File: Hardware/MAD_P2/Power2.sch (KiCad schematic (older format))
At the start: 39 parts, among them U13 XL1509-5.0, U14 XL1509-5.0, U15 AMS1117-3.3, U16 AMS1117-3.3, U17 AMS1117-3.3, U18 AMS1117-3.3

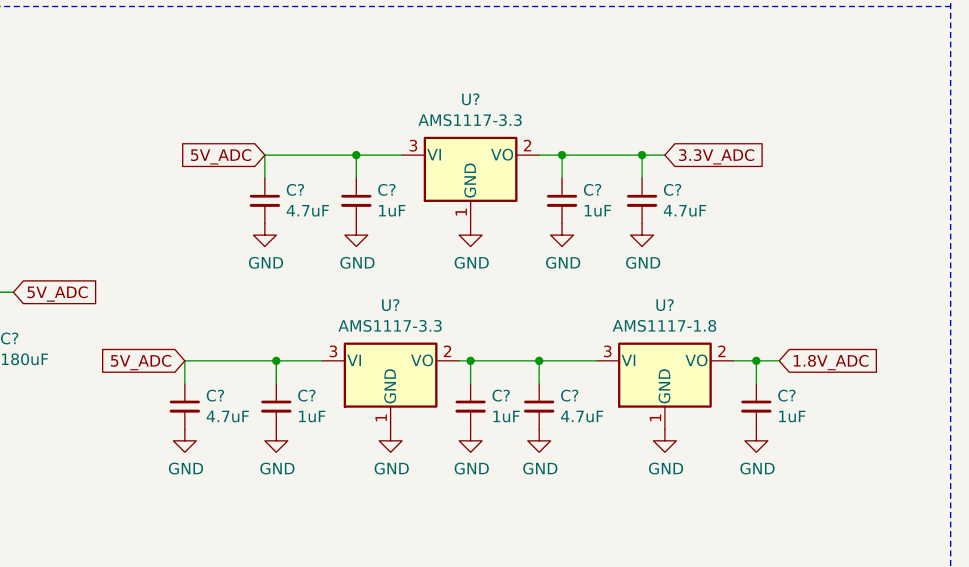
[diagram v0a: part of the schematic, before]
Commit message: changed adc to ads131
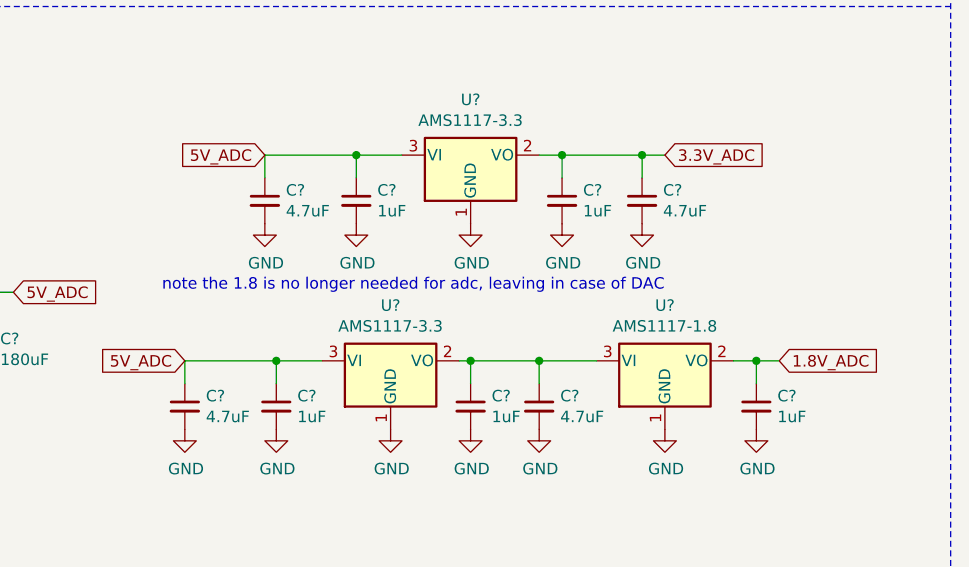
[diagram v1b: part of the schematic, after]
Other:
- note added: "note the 1.8 is no longer needed for adc, leaving in case of DAC"
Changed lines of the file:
@@
 Wire Notes Line
 	6950 500  6950 7800
+Text Notes 3500 6300 0    50   ~ 0
+note the 1.8 is no longer needed for adc, leaving in case of DAC
 $EndSCHEMATC

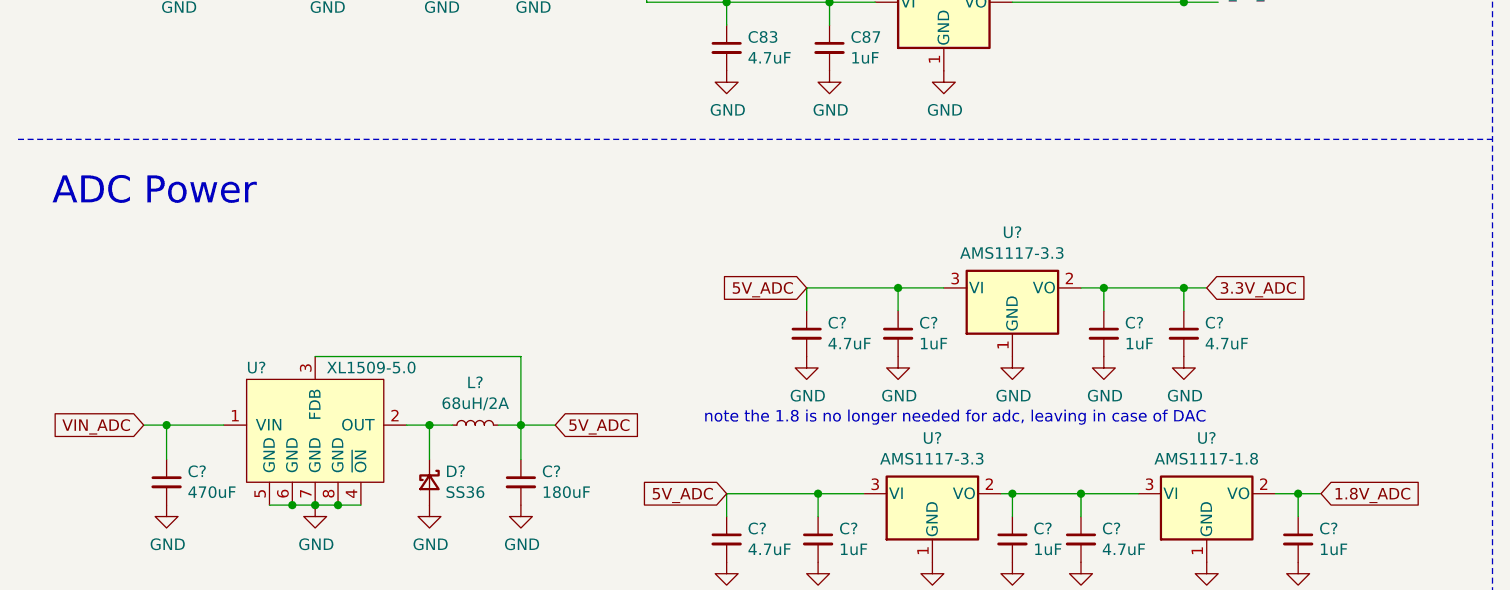
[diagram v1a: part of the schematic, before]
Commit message: finished adc, added dac
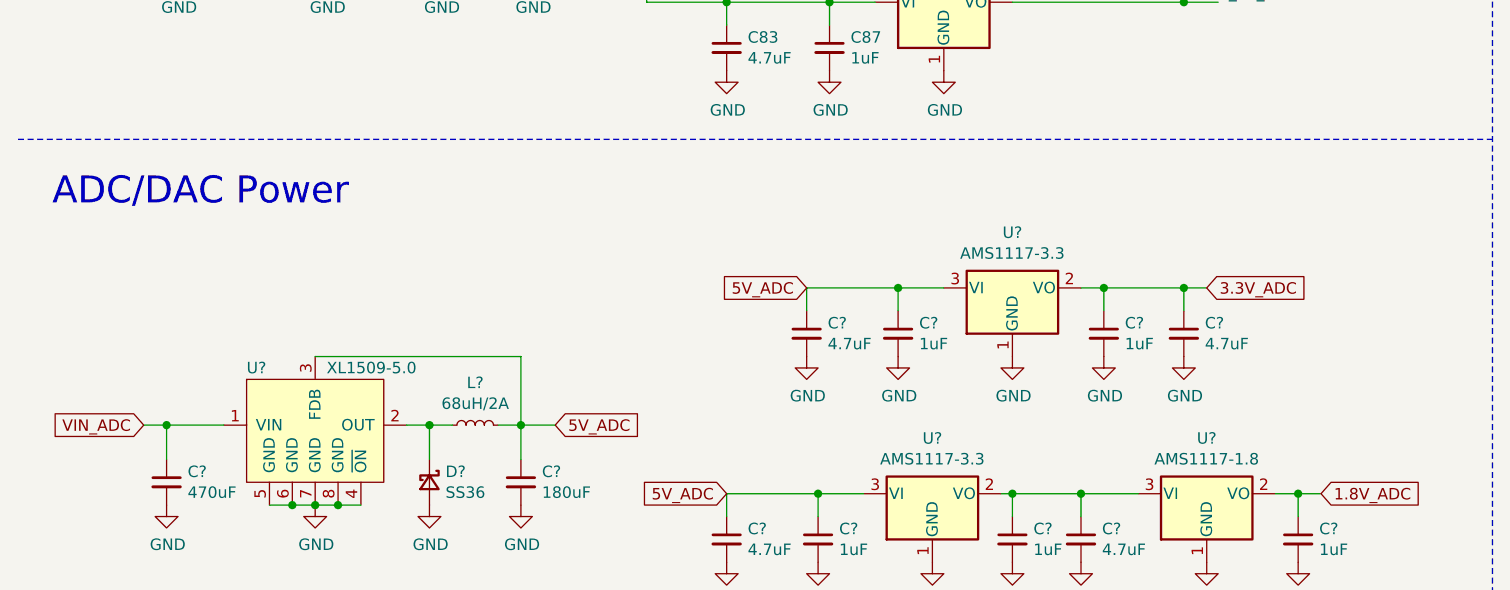
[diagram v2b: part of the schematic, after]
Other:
- note added: "ADC/DAC Power"
- note removed: "ADC Power"
- note removed: "note the 1.8 is no longer needed for adc, leaving in case of DAC"
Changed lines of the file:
@@
 $Descr A4 11693 8268
 encoding utf-8
-Sheet 3 6
+Sheet 3 7
 Title "MaD_P2"
 Date "2021-05-06"
@@
 	2700 6300 2850 6300
 Text Notes 650  5350 0    118  ~ 0
-ADC Power
+ADC/DAC Power
 Text GLabel 1050 6300 0    50   Input ~ 0
 VIN_ADC
@@
 Wire Notes Line
 	6950 500  6950 7800
-Text Notes 3500 6300 0    50   ~ 0
-note the 1.8 is no longer needed for adc, leaving in case of DAC
 $EndSCHEMATC

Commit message: began pcb layout
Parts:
- C100, C101, C102, C94, C95, C96, C97, C98, C99: renamed from C?; footprint (none) -> Capacitor_SMD:C_0603_1608Metric
- C76, C77: footprint (none) -> Capacitor_SMD:C_Elec_10x10.2
- C78, C79: footprint (none) -> Capacitor_SMD:C_Elec_6.3x7.7
- C80, C81, C82, C83, C84, C85, C86, C87: footprint (none) -> Capacitor_SMD:C_0603_1608Metric
- C92: renamed from C?; footprint (none) -> Capacitor_SMD:C_Elec_10x10.2
- C93: renamed from C?; footprint (none) -> Capacitor_SMD:C_Elec_6.3x7.7
- D10, D11: footprint (none) -> Diode_SMD:D_SMC
- D6: renamed from D?; footprint (none) -> Diode_SMD:D_SMC
- L10, L11: footprint (none) -> Inductor_SMD:L_10.4x10.4_H4.8
- L6: renamed from L?; footprint (none) -> Inductor_SMD:L_10.4x10.4_H4.8
- U13, U14: footprint (none) -> Package_SO:SOP-8_3.9x4.9mm_P1.27mm
- U22: renamed from U?; footprint (none) -> Package_SO:SOP-8_3.9x4.9mm_P1.27mm
- gave numbers to parts that had none: 3

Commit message: added lcsc part numbers to bom
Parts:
- C100, C102, C84, C85, C86, C87, C96, C97, C98: LCSC (none) -> C15849; TYPE (none) -> BASIC
- C101, C80, C81, C82, C83, C94, C95, C99: LCSC (none) -> C19666; TYPE (none) -> BASIC
- C76, C77, C92: LCSC (none) -> C3350; TYPE (none) -> EXT
- C78, C79, C93: LCSC (none) -> C413657; TYPE (none) -> EXT
- D10, D11, D6: LCSC (none) -> C35722; TYPE (none) -> BASIC
- L10, L11, L6: LCSC (none) -> C497902; TYPE (none) -> EXT
- U13, U14, U22: LCSC (none) -> C61063; TYPE (none) -> BASIC
- U15, U16, U17, U18, U23, U24: LCSC (none) -> C6186; TYPE (none) -> BASIC
- U25: LCSC (none) -> C6185; TYPE (none) -> EXT
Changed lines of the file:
@@
 F 2 "Capacitor_SMD:C_Elec_10x10.2" H 1200 2050 50  0001 C CNN
 F 3 "~" H 1200 2050 50  0001 C CNN
+F 4 "C3350" H 1200 2050 50  0001 C CNN "LCSC"
+F 5 "EXT" H 1200 2050 50  0001 C CNN "TYPE"
 	1    1200 2050
 	1    0    0    -1
@@
 F 2 "Package_SO:SOP-8_3.9x4.9mm_P1.27mm" H 1700 1800 50  0001 C CNN
 F 3 "" H 1700 1800 50  0001 C CNN
+F 4 "C61063" H 1850 1800 50  0001 C CNN "LCSC"
+F 5 "BASIC" H 1850 1800 50  0001 C CNN "TYPE"
 	1    1850 1800
 	1    0    0    -1
@@
 F 2 "Diode_SMD:D_SMC" V 2350 2050 50  0001 C CNN
 F 3 "~" V 2350 2050 50  0001 C CNN
+F 4 "C35722" H 2350 2050 50  0001 C CNN "LCSC"
+F 5 "BASIC" H 2350 2050 50  0001 C CNN "TYPE"
 	1    2350 2050
 	0    1    1    0
@@
 F 2 "Capacitor_SMD:C_Elec_6.3x7.7" H 2750 2050 50  0001 C CNN
 F 3 "~" H 2750 2050 50  0001 C CNN
+F 4 "C413657" H 2750 2050 50  0001 C CNN "LCSC"
+F 5 "EXT" H 2750 2050 50  0001 C CNN "TYPE"
 	1    2750 2050
 	1    0    0    -1
@@
 F 2 "Inductor_SMD:L_10.4x10.4_H4.8" H 2550 1800 50  0001 C CNN
 F 3 "~" H 2550 1800 50  0001 C CNN
+F 4 "C497902" H 2550 1800 50  0001 C CNN "LCSC"
+F 5 "EXT" H 2550 1800 50  0001 C CNN "TYPE"
 	1    2550 1800
 	0    -1   -1   0
@@
 F 2 "Package_TO_SOT_SMD:SOT-223-3_TabPin2" H 4550 1550 50  0001 C CNN
 F 3 "http://www.advanced-monolithic.com/pdf/ds1117.pdf" H 4650 1100 50  0001 C CNN
+F 4 "C6186" H 4550 1350 50  0001 C CNN "LCSC"
+F 5 "BASIC" H 4550 1350 50  0001 C CNN "TYPE"
 	1    4550 1350
 	1    0    0    -1
@@
 F 2 "Capacitor_SMD:C_0603_1608Metric" H 3600 1550 50  0001 C CNN
 F 3 "~" H 3600 1550 50  0001 C CNN
+F 4 "C19666" H 3600 1550 50  0001 C CNN "LCSC"
+F 5 "BASIC" H 3600 1550 50  0001 C CNN "TYPE"
 	1    3600 1550
 	1    0    0    -1
@@
 F 2 "Capacitor_SMD:C_0603_1608Metric" H 4050 1550 50  0001 C CNN
 F 3 "~" H 4050 1550 50  0001 C CNN
+F 4 "C15849" H 4050 1550 50  0001 C CNN "LCSC"
+F 5 "BASIC" H 4050 1550 50  0001 C CNN "TYPE"
 	1    4050 1550
 	1    0    0    -1
@@
 F 2 "Package_TO_SOT_SMD:SOT-223-3_TabPin2" H 4550 2500 50  0001 C CNN
 F 3 "http://www.advanced-monolithic.com/pdf/ds1117.pdf" H 4650 2050 50  0001 C CNN
+F 4 "C6186" H 4550 2300 50  0001 C CNN "LCSC"
+F 5 "BASIC" H 4550 2300 50  0001 C CNN "TYPE"
 	1    4550 2300
 	1    0    0    -1
@@
 F 2 "Capacitor_SMD:C_0603_1608Metric" H 3600 2500 50  0001 C CNN
 F 3 "~" H 3600 2500 50  0001 C CNN
+F 4 "C19666" H 3600 2500 50  0001 C CNN "LCSC"
+F 5 "BASIC" H 3600 2500 50  0001 C CNN "TYPE"
 	1    3600 2500
 	1    0    0    -1
@@
 F 2 "Capacitor_SMD:C_0603_1608Metric" H 4050 2500 50  0001 C CNN
 F 3 "~" H 4050 2500 50  0001 C CNN
+F 4 "C15849" H 4050 2500 50  0001 C CNN "LCSC"
+F 5 "BASIC" H 4050 2500 50  0001 C CNN "TYPE"
 	1    4050 2500
 	1    0    0    -1
@@
 F 2 "Capacitor_SMD:C_Elec_10x10.2" H 1200 4200 50  0001 C CNN
 F 3 "~" H 1200 4200 50  0001 C CNN
+F 4 "C3350" H 1200 4200 50  0001 C CNN "LCSC"
+F 5 "EXT" H 1200 4200 50  0001 C CNN "TYPE"
 	1    1200 4200
 	1    0    0    -1
@@
 F 2 "Package_SO:SOP-8_3.9x4.9mm_P1.27mm" H 1700 3950 50  0001 C CNN
 F 3 "" H 1700 3950 50  0001 C CNN
+F 4 "C61063" H 1850 3950 50  0001 C CNN "LCSC"
+F 5 "BASIC" H 1850 3950 50  0001 C CNN "TYPE"
 	1    1850 3950
 	1    0    0    -1
@@
 F 2 "Diode_SMD:D_SMC" V 2350 4200 50  0001 C CNN
 F 3 "~" V 2350 4200 50  0001 C CNN
+F 4 "C35722" H 2350 4200 50  0001 C CNN "LCSC"
+F 5 "BASIC" H 2350 4200 50  0001 C CNN "TYPE"
 	1    2350 4200
 	0    1    1    0
@@
 F 2 "Capacitor_SMD:C_Elec_6.3x7.7" H 2750 4200 50  0001 C CNN
 F 3 "~" H 2750 4200 50  0001 C CNN
+F 4 "C413657" H 2750 4200 50  0001 C CNN "LCSC"
+F 5 "EXT" H 2750 4200 50  0001 C CNN "TYPE"
 	1    2750 4200
 	1    0    0    -1
@@
 F 2 "Inductor_SMD:L_10.4x10.4_H4.8" H 2550 3950 50  0001 C CNN
 F 3 "~" H 2550 3950 50  0001 C CNN
+F 4 "C497902" H 2550 3950 50  0001 C CNN "LCSC"
+F 5 "EXT" H 2550 3950 50  0001 C CNN "TYPE"
 	1    2550 3950
 	0    -1   -1   0
@@
 F 2 "Package_TO_SOT_SMD:SOT-223-3_TabPin2" H 4550 3700 50  0001 C CNN
 F 3 "http://www.advanced-monolithic.com/pdf/ds1117.pdf" H 4650 3250 50  0001 C CNN
+F 4 "C6186" H 4550 3500 50  0001 C CNN "LCSC"
+F 5 "BASIC" H 4550 3500 50  0001 C CNN "TYPE"
 	1    4550 3500
 	1    0    0    -1
@@
 F 2 "Capacitor_SMD:C_0603_1608Metric" H 3600 3700 50  0001 C CNN
 F 3 "~" H 3600 3700 50  0001 C CNN
+F 4 "C19666" H 3600 3700 50  0001 C CNN "LCSC"
+F 5 "BASIC" H 3600 3700 50  0001 C CNN "TYPE"
 	1    3600 3700
 	1    0    0    -1
@@
 F 2 "Capacitor_SMD:C_0603_1608Metric" H 4050 3700 50  0001 C CNN
 F 3 "~" H 4050 3700 50  0001 C CNN
+F 4 "C15849" H 4050 3700 50  0001 C CNN "LCSC"
+F 5 "BASIC" H 4050 3700 50  0001 C CNN "TYPE"
 	1    4050 3700
 	1    0    0    -1
@@
 F 2 "Package_TO_SOT_SMD:SOT-223-3_TabPin2" H 4550 4650 50  0001 C CNN
 F 3 "http://www.advanced-monolithic.com/pdf/ds1117.pdf" H 4650 4200 50  0001 C CNN
+F 4 "C6186" H 4550 4450 50  0001 C CNN "LCSC"
+F 5 "BASIC" H 4550 4450 50  0001 C CNN "TYPE"
 	1    4550 4450
 	1    0    0    -1
@@
 F 2 "Capacitor_SMD:C_0603_1608Metric" H 3600 4650 50  0001 C CNN
 F 3 "~" H 3600 4650 50  0001 C CNN
+F 4 "C19666" H 3600 4650 50  0001 C CNN "LCSC"
+F 5 "BASIC" H 3600 4650 50  0001 C CNN "TYPE"
 	1    3600 4650
 	1    0    0    -1
@@
 F 2 "Capacitor_SMD:C_0603_1608Metric" H 4050 4650 50  0001 C CNN
 F 3 "~" H 4050 4650 50  0001 C CNN
+F 4 "C15849" H 4050 4650 50  0001 C CNN "LCSC"
+F 5 "BASIC" H 4050 4650 50  0001 C CNN "TYPE"
 	1    4050 4650
 	1    0    0    -1
@@
 F 2 "Capacitor_SMD:C_Elec_10x10.2" H 1150 6550 50  0001 C CNN
 F 3 "~" H 1150 6550 50  0001 C CNN
+F 4 "C3350" H 1150 6550 50  0001 C CNN "LCSC"
+F 5 "EXT" H 1150 6550 50  0001 C CNN "TYPE"
 	1    1150 6550
 	1    0    0    -1
@@
 F 2 "Package_SO:SOP-8_3.9x4.9mm_P1.27mm" H 1650 6300 50  0001 C CNN
 F 3 "" H 1650 6300 50  0001 C CNN
+F 4 "C61063" H 1800 6300 50  0001 C CNN "LCSC"
+F 5 "BASIC" H 1800 6300 50  0001 C CNN "TYPE"
 	1    1800 6300
 	1    0    0    -1
@@
 F 2 "Diode_SMD:D_SMC" V 2300 6550 50  0001 C CNN
 F 3 "~" V 2300 6550 50  0001 C CNN
+F 4 "C35722" H 2300 6550 50  0001 C CNN "LCSC"
+F 5 "BASIC" H 2300 6550 50  0001 C CNN "TYPE"
 	1    2300 6550
 	0    1    1    0
@@
 F 2 "Capacitor_SMD:C_Elec_6.3x7.7" H 2700 6550 50  0001 C CNN
 F 3 "~" H 2700 6550 50  0001 C CNN
+F 4 "C413657" H 2700 6550 50  0001 C CNN "LCSC"
+F 5 "EXT" H 2700 6550 50  0001 C CNN "TYPE"
 	1    2700 6550
 	1    0    0    -1
@@
 F 2 "Inductor_SMD:L_10.4x10.4_H4.8" H 2500 6300 50  0001 C CNN
 F 3 "~" H 2500 6300 50  0001 C CNN
+F 4 "C497902" H 2500 6300 50  0001 C CNN "LCSC"
+F 5 "EXT" H 2500 6300 50  0001 C CNN "TYPE"
 	1    2500 6300
 	0    -1   -1   0
@@
 F 2 "Package_TO_SOT_SMD:SOT-223-3_TabPin2" H 4850 5900 50  0001 C CNN
 F 3 "http://www.advanced-monolithic.com/pdf/ds1117.pdf" H 4950 5450 50  0001 C CNN
+F 4 "C6186" H 4850 5700 50  0001 C CNN "LCSC"
+F 5 "BASIC" H 4850 5700 50  0001 C CNN "TYPE"
 	1    4850 5700
 	1    0    0    -1
@@
 F 2 "Capacitor_SMD:C_0603_1608Metric" H 4350 5900 50  0001 C CNN
 F 3 "~" H 4350 5900 50  0001 C CNN
+F 4 "C15849" H 4350 5900 50  0001 C CNN "LCSC"
+F 5 "BASIC" H 4350 5900 50  0001 C CNN "TYPE"
 	1    4350 5900
 	1    0    0    -1
@@
 F 2 "Capacitor_SMD:C_0603_1608Metric" H 3950 5900 50  0001 C CNN
 F 3 "~" H 3950 5900 50  0001 C CNN
+F 4 "C19666" H 3950 5900 50  0001 C CNN "LCSC"
+F 5 "BASIC" H 3950 5900 50  0001 C CNN "TYPE"
 	1    3950 5900
 	1    0    0    -1
@@
 F 2 "Capacitor_SMD:C_0603_1608Metric" H 5250 5900 50  0001 C CNN
 F 3 "~" H 5250 5900 50  0001 C CNN
+F 4 "C15849" H 5250 5900 50  0001 C CNN "LCSC"
+F 5 "BASIC" H 5250 5900 50  0001 C CNN "TYPE"
 	1    5250 5900
 	1    0    0    -1
@@
 F 2 "Package_TO_SOT_SMD:SOT-223-3_TabPin2" H 5700 6800 50  0001 C CNN
 F 3 "http://www.advanced-monolithic.com/pdf/ds1117.pdf" H 5800 6350 50  0001 C CNN
+F 4 "C6185" H 5700 6600 50  0001 C CNN "LCSC"
+F 5 "EXT" H 5700 6600 50  0001 C CNN "TYPE"
 	1    5700 6600
 	1    0    0    -1
@@
 F 2 "Package_TO_SOT_SMD:SOT-223-3_TabPin2" H 4500 6800 50  0001 C CNN
 F 3 "http://www.advanced-monolithic.com/pdf/ds1117.pdf" H 4600 6350 50  0001 C CNN
+F 4 "C6186" H 4500 6600 50  0001 C CNN "LCSC"
+F 5 "BASIC" H 4500 6600 50  0001 C CNN "TYPE"
 	1    4500 6600
 	1    0    0    -1
@@
 F 2 "Capacitor_SMD:C_0603_1608Metric" H 4850 6800 50  0001 C CNN
 F 3 "~" H 4850 6800 50  0001 C CNN
+F 4 "C15849" H 4850 6800 50  0001 C CNN "LCSC"
+F 5 "BASIC" H 4850 6800 50  0001 C CNN "TYPE"
 	1    4850 6800
 	1    0    0    -1
@@
 F 2 "Capacitor_SMD:C_0603_1608Metric" H 5150 6800 50  0001 C CNN
 F 3 "~" H 5150 6800 50  0001 C CNN
+F 4 "C19666" H 5150 6800 50  0001 C CNN "LCSC"
+F 5 "BASIC" H 5150 6800 50  0001 C CNN "TYPE"
 	1    5150 6800
 	1    0    0    -1
@@
 F 2 "Capacitor_SMD:C_0603_1608Metric" H 4000 6800 50  0001 C CNN
 F 3 "~" H 4000 6800 50  0001 C CNN
+F 4 "C15849" H 4000 6800 50  0001 C CNN "LCSC"
+F 5 "BASIC" H 4000 6800 50  0001 C CNN "TYPE"
 	1    4000 6800
 	1    0    0    -1
@@
 F 2 "Capacitor_SMD:C_0603_1608Metric" H 3600 6800 50  0001 C CNN
 F 3 "~" H 3600 6800 50  0001 C CNN
+F 4 "C19666" H 3600 6800 50  0001 C CNN "LCSC"
+F 5 "BASIC" H 3600 6800 50  0001 C CNN "TYPE"
 	1    3600 6800
 	1    0    0    -1
@@
 F 2 "Capacitor_SMD:C_0603_1608Metric" H 5600 5900 50  0001 C CNN
 F 3 "~" H 5600 5900 50  0001 C CNN
+F 4 "C19666" H 5600 5900 50  0001 C CNN "LCSC"
+F 5 "BASIC" H 5600 5900 50  0001 C CNN "TYPE"
 	1    5600 5900
 	1    0    0    -1
@@
 F 2 "Capacitor_SMD:C_0603_1608Metric" H 6100 6800 50  0001 C CNN
 F 3 "~" H 6100 6800 50  0001 C CNN
+F 4 "C15849" H 6100 6800 50  0001 C CNN "LCSC"
+F 5 "BASIC" H 6100 6800 50  0001 C CNN "TYPE"
 	1    6100 6800
 	1    0    0    -1
